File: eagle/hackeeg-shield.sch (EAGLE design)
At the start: 142 parts, among them IC1 ADS1299IPAG, IC10 TXB0108PWR, IC11 TXB0108PWR, IC2 TPS72325DBVT, IC3 TPS73225DBVT, IC5 24AA256UID, IC6 TPS60403DBVT, IC7 OPA376DBV, IC8 OPA376DBV, IC9 TXS0102DCUR

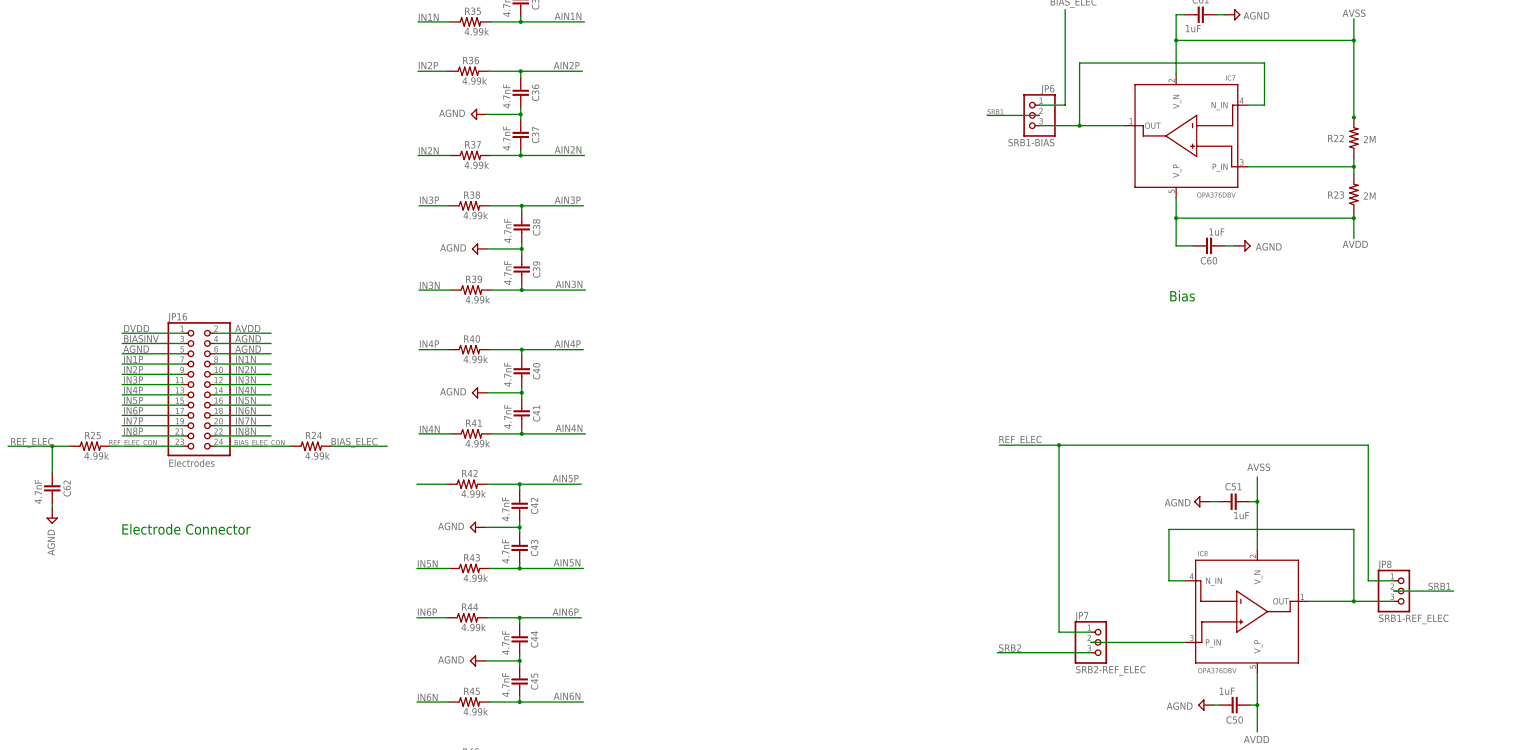
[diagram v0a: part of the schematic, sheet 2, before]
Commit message: replaced electrode connector with new connector
- On Shore Technologies male shrouded header OS302-R241.lbr
- to match cable connectors
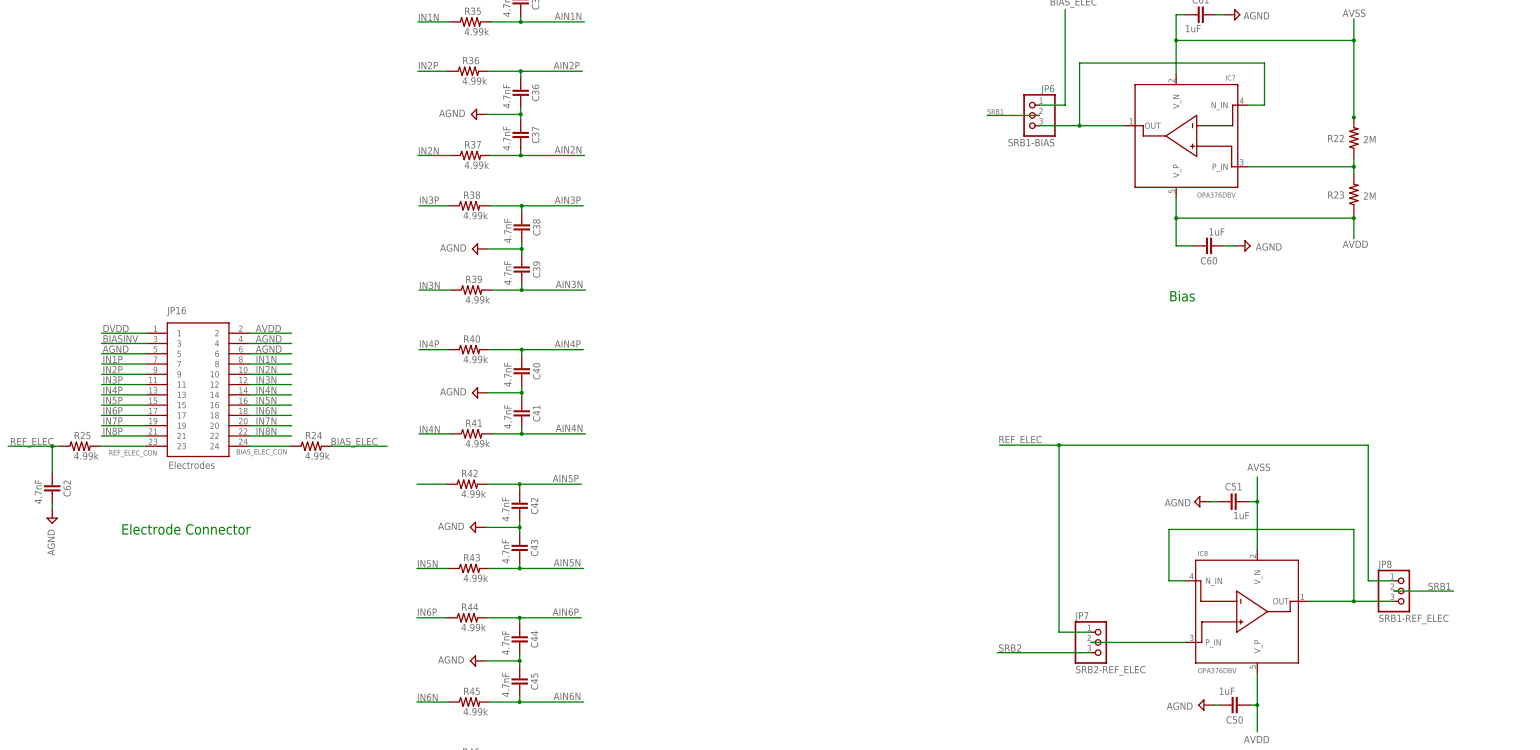
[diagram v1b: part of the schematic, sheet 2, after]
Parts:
- JP16: device headers:PINHD-2X12 -> OS302-R241:302-R241
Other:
- note added: "v1.4.1"
- note removed: "v1.4.0"
- moved on the sheet: R25

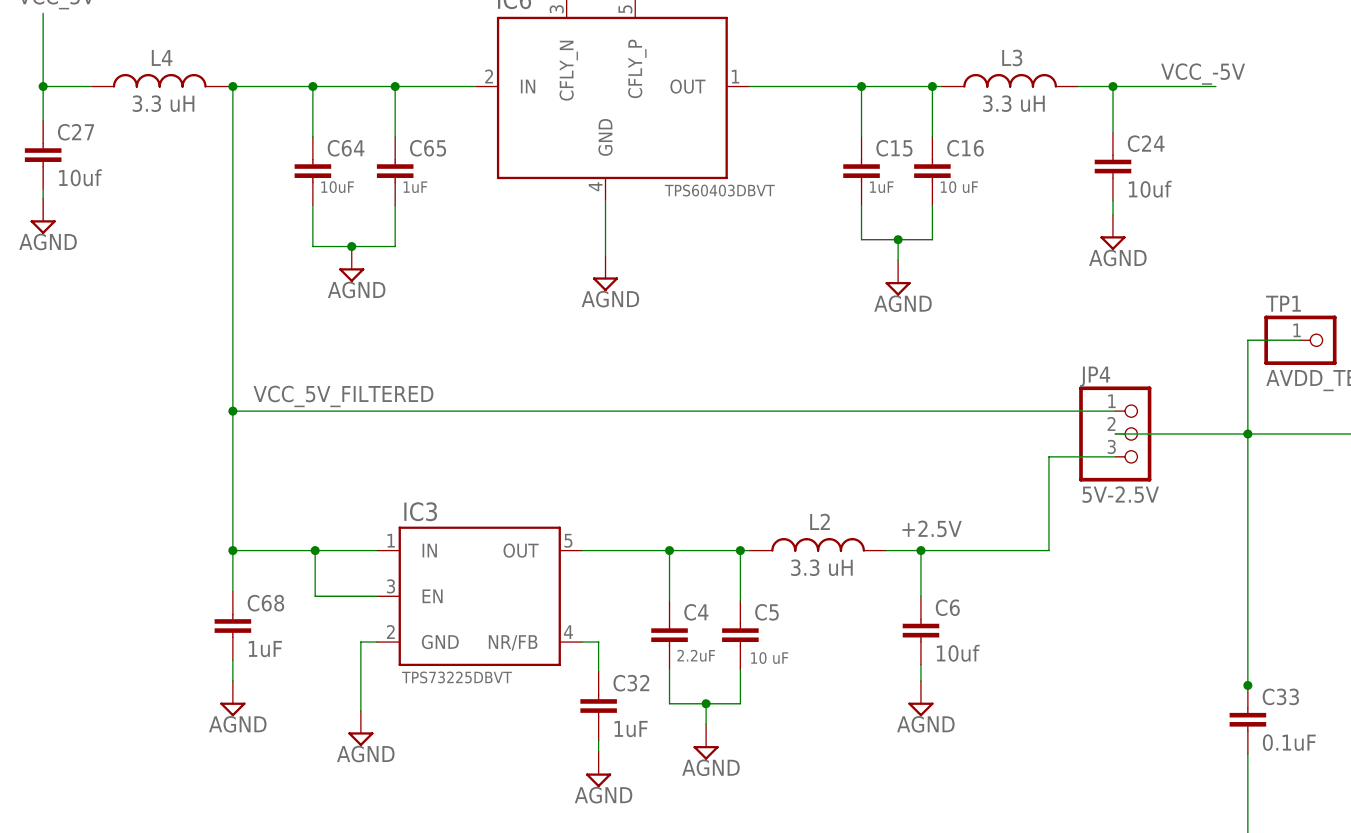
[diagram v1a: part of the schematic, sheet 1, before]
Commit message: minor routing updates, delete airwires
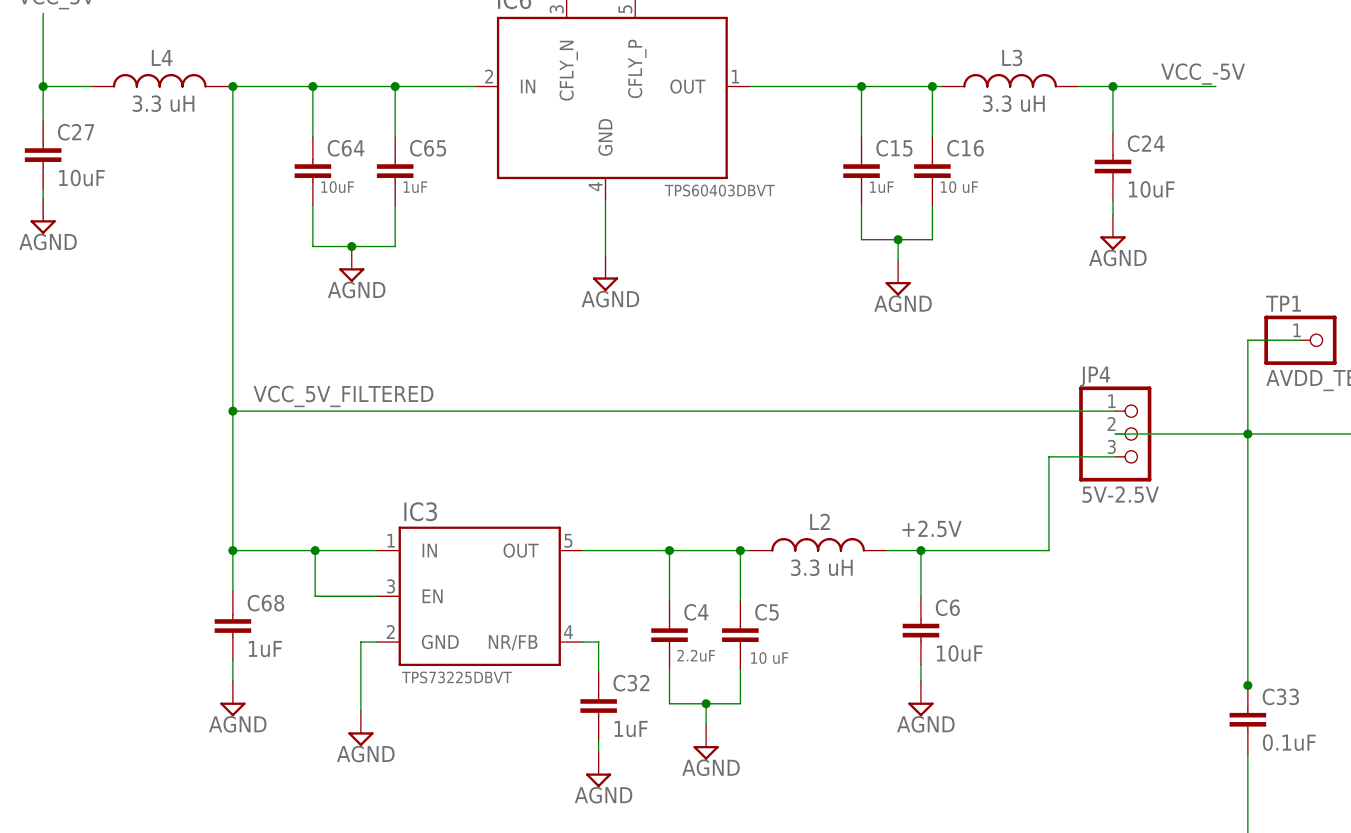
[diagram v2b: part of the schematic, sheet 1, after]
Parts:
- C24, C27, C6: value 10uf -> 10uF
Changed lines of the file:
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@@
 <part name="C4" library="SparkFun-Passives" deviceset="CAP" device="0603-CAP" value="2.2uF"/>
 <part name="C5" library="SparkFun-Passives" deviceset="CAP" device="0603-CAP" value="10 uF"/>
-<part name="C6" library="SparkFun-Passives" deviceset="CAP" device="0603-CAP" value="10uf"/>
+<part name="C6" library="SparkFun-Passives" deviceset="CAP" device="0603-CAP" value="10uF"/>
 <part name="C7" library="SparkFun-Passives" deviceset="CAP" device="0603-CAP" value="1uF"/>
 <part name="C8" library="SparkFun-Passives" deviceset="CAP" device="0603-CAP" value="0.1uF"/>
@@
 <part name="C15" library="SparkFun-Passives" deviceset="CAP" device="0603-CAP" value="1uF"/>
 <part name="C16" library="SparkFun-Passives" deviceset="CAP" device="0603-CAP" value="10 uF"/>
-<part name="C24" library="SparkFun-Passives" deviceset="CAP" device="0603-CAP" value="10uf"/>
+<part name="C24" library="SparkFun-Passives" deviceset="CAP" device="0603-CAP" value="10uF"/>
 <part name="SUPPLY1" library="supply2" deviceset="AGND" device=""/>
 <part name="SUPPLY9" library="supply2" deviceset="AGND" device=""/>
@@
 <part name="C26" library="SparkFun-Passives" deviceset="CAP" device="0603-CAP" value="1uF"/>
 <part name="L4" library="SparkFun-Passives" deviceset="INDUCTOR" device="0805" value="3.3 uH"/>
-<part name="C27" library="SparkFun-Passives" deviceset="CAP" device="0603-CAP" value="10uf"/>
+<part name="C27" library="SparkFun-Passives" deviceset="CAP" device="0603-CAP" value="10uF"/>
 <part name="SUPPLY12" library="supply2" deviceset="AGND" device=""/>
 <part name="C28" library="SparkFun-Passives" deviceset="CAP" device="0603-CAP" value="2.2uF"/>

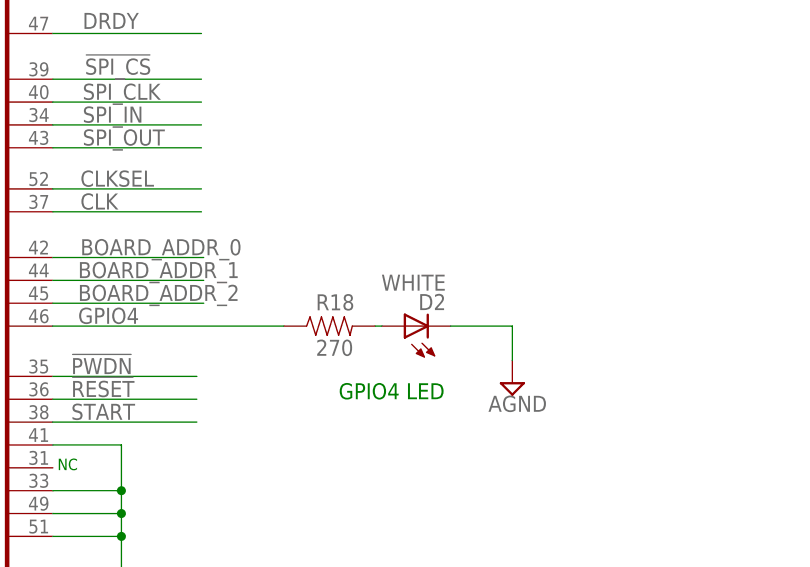
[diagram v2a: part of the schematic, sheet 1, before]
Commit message: updated HackEEG version number on PCB to 1.4.2 GA
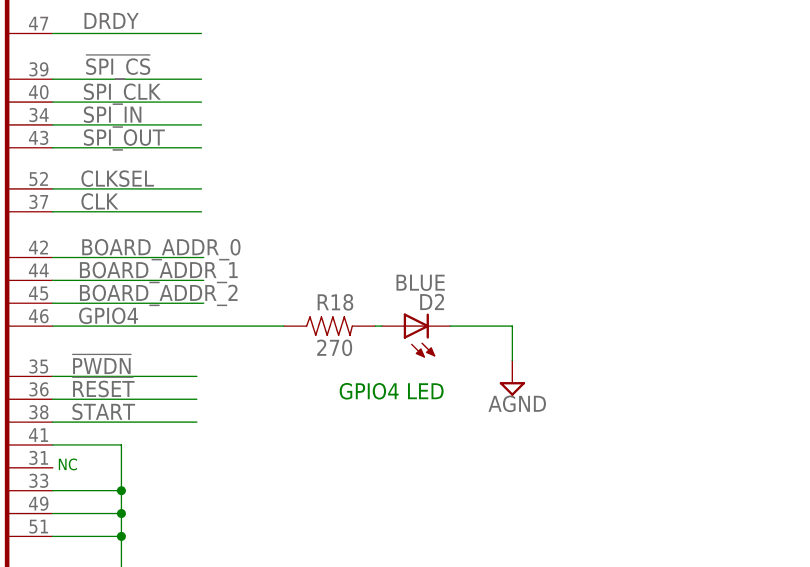
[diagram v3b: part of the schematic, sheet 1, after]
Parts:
- D2: value WHITE -> BLUE
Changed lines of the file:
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@@
 <part name="R18" library="SparkFun-Passives" deviceset="RESISTOR" device="0603-RES" value="270"/>
 <part name="SUPPLY40" library="supply2" deviceset="AGND" device=""/>
-<part name="D2" library="SparkFun-LED" deviceset="LED-WHITE" device="" value="WHITE"/>
+<part name="D2" library="SparkFun-LED" deviceset="LED-WHITE" device="" value="BLUE"/>
 <part name="IC5" library="microchip" deviceset="24*" device="SN" technology="LC256" value="24AA256UID"/>
 <part name="R19" library="SparkFun-Passives" deviceset="RESISTOR" device="0603-RES" value="10k"/>

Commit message: bump schematic version to 1.4.2 to match PCB
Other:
- note added: "v1.4.2"
- note removed: "v1.4.1"
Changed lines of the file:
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@@
 By-Attribution Share-Alike 4.0 license</text>
 <text x="328.676" y="37.592" size="2.54" layer="95">Copyright 2014-2018 Adam Feuer</text>
-<text x="414.782" y="6.858" size="2.1844" layer="95">v1.4.1</text>
+<text x="414.782" y="6.858" size="2.1844" layer="95">v1.4.2</text>
 <text x="246.634" y="212.344" size="1.778" layer="91">NC</text>
 <text x="327.406" y="161.798" size="1.27" layer="91">NC</text>

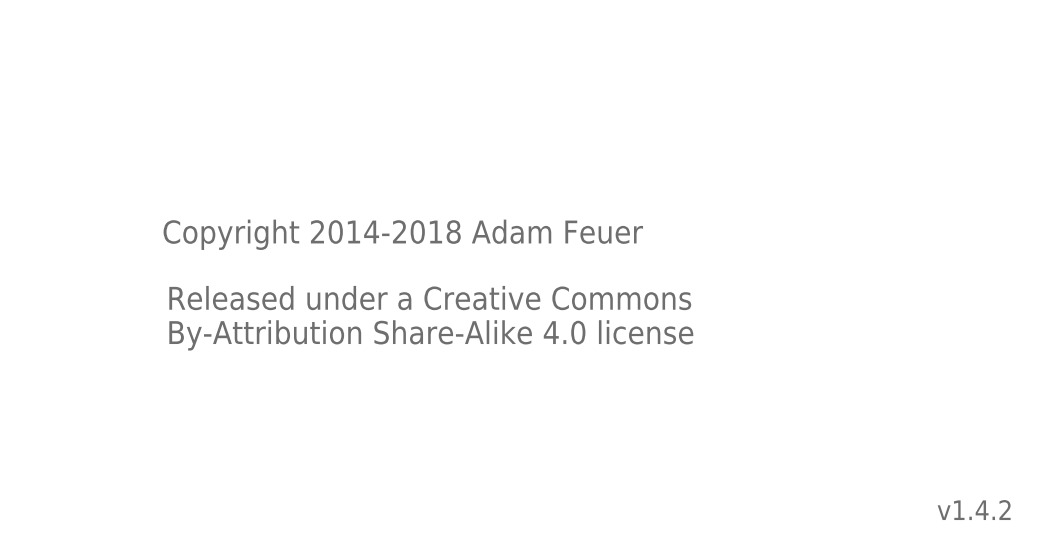
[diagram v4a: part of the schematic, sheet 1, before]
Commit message: relicense to CERN OHL 1.2 - hackeeg-shield sch and brd
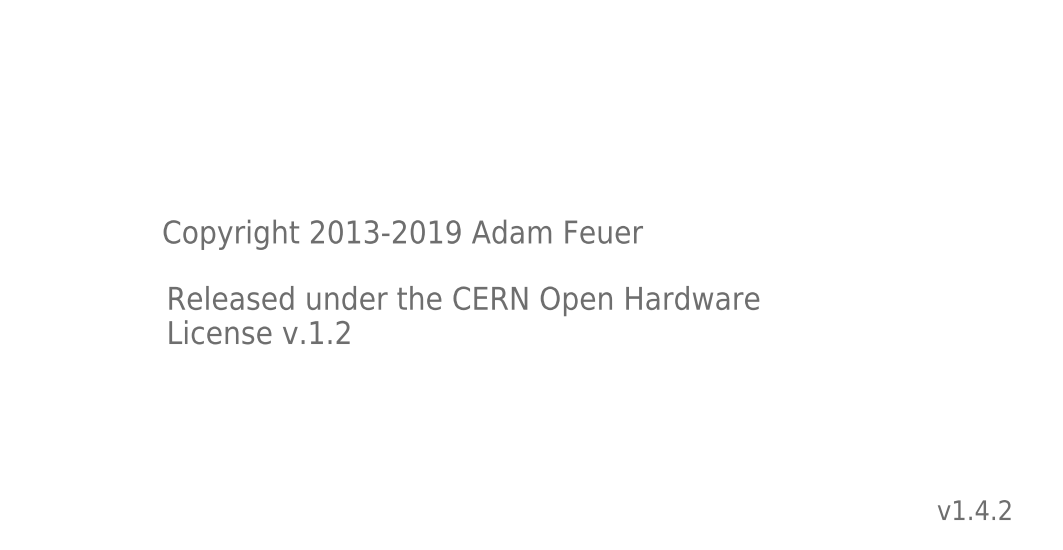
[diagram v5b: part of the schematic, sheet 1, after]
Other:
- note added: "Copyright 2013-2019 Adam Feuer"
- note added: "Released under the CERN Open Hardware License v.1.2"
- note removed: "Copyright 2014-2018 Adam Feuer"
- note removed: "Released under a Creative Commons By-Attribution Share-Alike 4.0 license"
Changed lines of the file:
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@@
 <text x="246.634" y="218.186" size="1.778" layer="91">NC</text>
 <text x="246.634" y="215.392" size="1.778" layer="91">NC</text>
-<text x="329.184" y="26.416" size="2.54" layer="95">Released under a Creative Commons
-By-Attribution Share-Alike 4.0 license</text>
-<text x="328.676" y="37.592" size="2.54" layer="95">Copyright 2014-2018 Adam Feuer</text>
+<text x="329.184" y="26.416" size="2.54" layer="95">Released under the CERN Open Hardware
+License v.1.2</text>
+<text x="328.676" y="37.592" size="2.54" layer="95">Copyright 2013-2019 Adam Feuer</text>
 <text x="414.782" y="6.858" size="2.1844" layer="95">v1.4.2</text>
 <text x="246.634" y="212.344" size="1.778" layer="91">NC</text>
@@
 <text x="284.734" y="62.484" size="2.54" layer="91">Stimulus-Response Buffer (SRB)</text>
 <text x="293.116" y="179.324" size="2.54" layer="91">Bias</text>
-<text x="320.802" y="26.416" size="2.54" layer="95">Released under a Creative Commons
-By-Attribution Share-Alike 4.0 license</text>
-<text x="320.294" y="37.592" size="2.54" layer="95">Copyright 2014-2018 Adam Feuer</text>
+<text x="320.802" y="26.416" size="2.54" layer="95">Released under the CERN Open Hardware
+License v.1.2</text>
+<text x="320.294" y="37.592" size="2.54" layer="95">Copyright 2013-2019 Adam Feuer</text>
 <text x="65.532" y="264.668" size="2.54" layer="91">Input Filtering</text>
 <text x="160.274" y="254.762" size="2.54" layer="91">(This side to ADS1299 inputs)</text>
@@
 positions for
 jumper storage)</text>
-<text x="326.136" y="26.416" size="2.54" layer="95">Released under a Creative Commons
-By-Attribution Share-Alike 4.0 license</text>
-<text x="325.628" y="37.592" size="2.54" layer="95">Copyright 2014-2018 Adam Feuer</text>
+<text x="326.136" y="26.416" size="2.54" layer="95">Released under the CERN Open Hardware
+License v.1.2</text>
+<text x="325.628" y="37.592" size="2.54" layer="95">Copyright 2013-2019 Adam Feuer</text>
 <text x="315.468" y="84.582" size="2.54" layer="91">Shield Connectors</text>
 <text x="356.616" y="254" size="1.524" layer="91">SCL1</text>

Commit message: update copper copyright notice
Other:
- note added: "Copyright 2013-2020 Adam Feuer"
- note added: "v1.5.0"
- note removed: "Copyright 2013-2019 Adam Feuer"
- note removed: "v1.4.2"
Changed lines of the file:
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@@
 <?xml version="1.0" encoding="utf-8"?>
 <!DOCTYPE eagle SYSTEM "eagle.dtd">
-<eagle version="9.4.0">
+<eagle version="9.5.2">
 <drawing>
 <settings>
@@
 <text x="329.184" y="26.416" size="2.54" layer="95">Released under the CERN Open Hardware
 License v.1.2</text>
-<text x="328.676" y="37.592" size="2.54" layer="95">Copyright 2013-2019 Adam Feuer</text>
-<text x="414.782" y="6.858" size="2.1844" layer="95">v1.4.2</text>
+<text x="328.676" y="37.592" size="2.54" layer="95">Copyright 2013-2020 Adam Feuer</text>
+<text x="414.782" y="6.858" size="2.1844" layer="95">v1.5.0</text>
 <text x="246.634" y="212.344" size="1.778" layer="91">NC</text>
 <text x="327.406" y="161.798" size="1.27" layer="91">NC</text>
@@
 <text x="320.802" y="26.416" size="2.54" layer="95">Released under the CERN Open Hardware
 License v.1.2</text>
-<text x="320.294" y="37.592" size="2.54" layer="95">Copyright 2013-2019 Adam Feuer</text>
+<text x="81.534" y="111.252" size="2.54" layer="95">Copyright 2013-2020 Adam Feuer</text>
 <text x="65.532" y="264.668" size="2.54" layer="91">Input Filtering</text>
 <text x="160.274" y="254.762" size="2.54" layer="91">(This side to ADS1299 inputs)</text>
@@
 <text x="326.136" y="26.416" size="2.54" layer="95">Released under the CERN Open Hardware
 License v.1.2</text>
-<text x="325.628" y="37.592" size="2.54" layer="95">Copyright 2013-2019 Adam Feuer</text>
+<text x="325.628" y="37.592" size="2.54" layer="95">Copyright 2013-2020 Adam Feuer</text>
 <text x="315.468" y="84.582" size="2.54" layer="91">Shield Connectors</text>
 <text x="356.616" y="254" size="1.524" layer="91">SCL1</text>
